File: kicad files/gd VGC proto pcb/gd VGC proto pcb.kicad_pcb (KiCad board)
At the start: 4 copper layers, 114.3 x 73.7 mm, 117 parts, among them J1 +5V_IN, J10 VID_OUT, J11 RCA MONO OUT, J12 Main Data Bus, J13 COMSYNC, J14 Mono-Color, J15 VBL, J16 RTC, J17 RCA Shunt Select, J18 RCA, J19 CREF, J2 Video Binary B, J20 RGB In, J21 CLK_14M, J22 Memory Control, J23 VGC Extra, J24 CLK_PH0, J25 Bald-Ext-1, J26 SYNC, J27 12V_IN, J28 -5V_In, J3 Aux Data Bus, J4 DAC RGB, J5 Video Binary G, J6 COMP_RGB, J7 Video Binary R, J8 RAM Addr Bus, J9 Composite Sync, Q1 BC817, Q2 BC817, Q3 BC817, U1 MIC5504-3.3YM5, U2 28.636360 MHz

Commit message: revision 1 routed and ready for fab
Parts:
- added REF**: OSHW-Logo2_7.3x6mm_SilkScreen, Symbol:OSHW-Logo2_7.3x6mm_SilkScreen, B.Cu at (190.5, 130.8)
- added REF**: KiCad-Logo2_5mm_SilkScreen, Symbol:KiCad-Logo2_5mm_SilkScreen, B.Cu at (152.4, 88.9)
- added svg2mod: G***, My Libraries:BE5v2, B.Cu at (172.7, 119.4)
- TP5: moved to B.Cu
- moved TF1 1.30 mm to (187.8, 115.2)
- moved TP5 1.28 mm to (95.8, 83.1)
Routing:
- net /R8-2: track 3.35 -> 2.57 mm
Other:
- board text added: "+12V"
- board text added: "+5V"
- board text added: "-5V"
- board text added: "0"
- board text added: "1"
- board text added: "1 1"
- board text added: "10"
- board text added: "11"
- board text added: "14M"
- board text added: "2"
- board text added: "28M"
- board text added: "3"
- board text added: "3.5DIK"
- board text added: "4"
- board text added: "5"
- board text added: "5V"
- board text added: "6"
- board text added: "7"
- board text added: "8"
- board text added: "9"
- board text added: "A2RW"
- board text added: "AD"
- board text added: "AD0"
- board text added: "AD1"
- board text added: "AD2"
- board text added: "AD3"
- board text added: "AD4"
- board text added: "AD5"
- board text added: "AD6"
- board text added: "AD7"
- board text added: "Aux Data"
- board text added: "BAUS12"
- board text added: "CBLU"
- board text added: "CGRN"
- board text added: "COM SYNC"
- board text added: "COM- SYNC"
- board text added: "COMP- SYN"
- board text added: "COMP_SYN"
- board text added: "CRED"
- board text added: "CREF.H"
- board text added: "CREF.L"
- board text added: "CSYN"
- board text added: "FLIP6"
- board text added: "Flip6"
- board text added: "Flip7"
- board text added: "Golden Delicious VGC Proto PCB v1 @baldengineer rev1"
- board text added: "H2"
- board text added: "H2-1"
- board text added: "H2-6"
- board text added: "H3"
- board text added: "H3-1"
- board text added: "H3-6"
- board text added: "H4"
- board text added: "H4-1"
- board text added: "H4-6"
- board text added: "HDSEL"
- board text added: "Hi Chat! Thank You! *rj was right"
- board text added: "IRQ"
- board text added: "L12"
- board text added: "L3"
- board text added: "L4"
- board text added: "M2SEL"
- board text added: "MC"
- board text added: "MD"
- board text added: "MD0"
- board text added: "MD1"
- board text added: "MD2"
- board text added: "MD3"
- board text added: "MD4"
- board text added: "MD5"
- board text added: "MD6"
- board text added: "MD7"
- board text added: "Main Data"
- board text added: "Mono Color"
- board text added: "N/C"
- board text added: "PH0"
- board text added: "RA"
- board text added: "RA0"
- board text added: "RA1"
- board text added: "RA2"
- board text added: "RA3"
- board text added: "RA4"
- board text added: "RA5"
- board text added: "RA6"
- board text added: "RA7"
- board text added: "RAM Addr"
- board text added: "RCA Out"
- board text added: "RCA Shunt"
- board text added: "RESET"
- board text added: "RGB"
- board text added: "RGB1"
- board text added: "RGB2"
- board text added: "RGB4"
- board text added: "RGB8"
- board text added: "RW"
- board text added: "STRETCH"
- board text added: "SYNC"
- board text added: "Stretch"
- board text added: "UC2-10"
- board text added: "UC2-3"
- board text added: "UC2-4"
- board text added: "UC2-5"
- board text added: "UG3-1"
- board text added: "UG3-5"
- board text added: "UG3-6"
- board text added: "UG3-7"
- board text added: "VBL"
- board text added: "VBL.L"
- board text added: "VID"

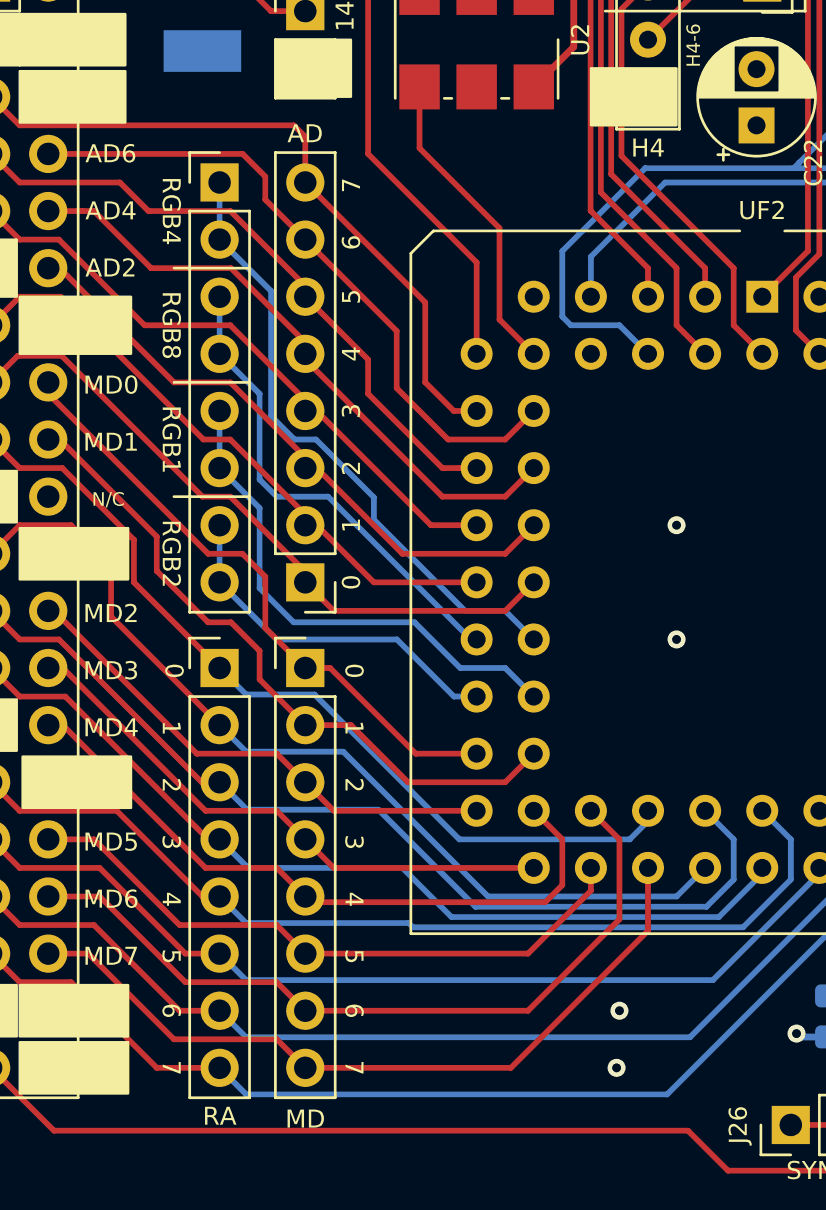
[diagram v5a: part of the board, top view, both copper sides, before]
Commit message: added some small vias for GND pours that missed
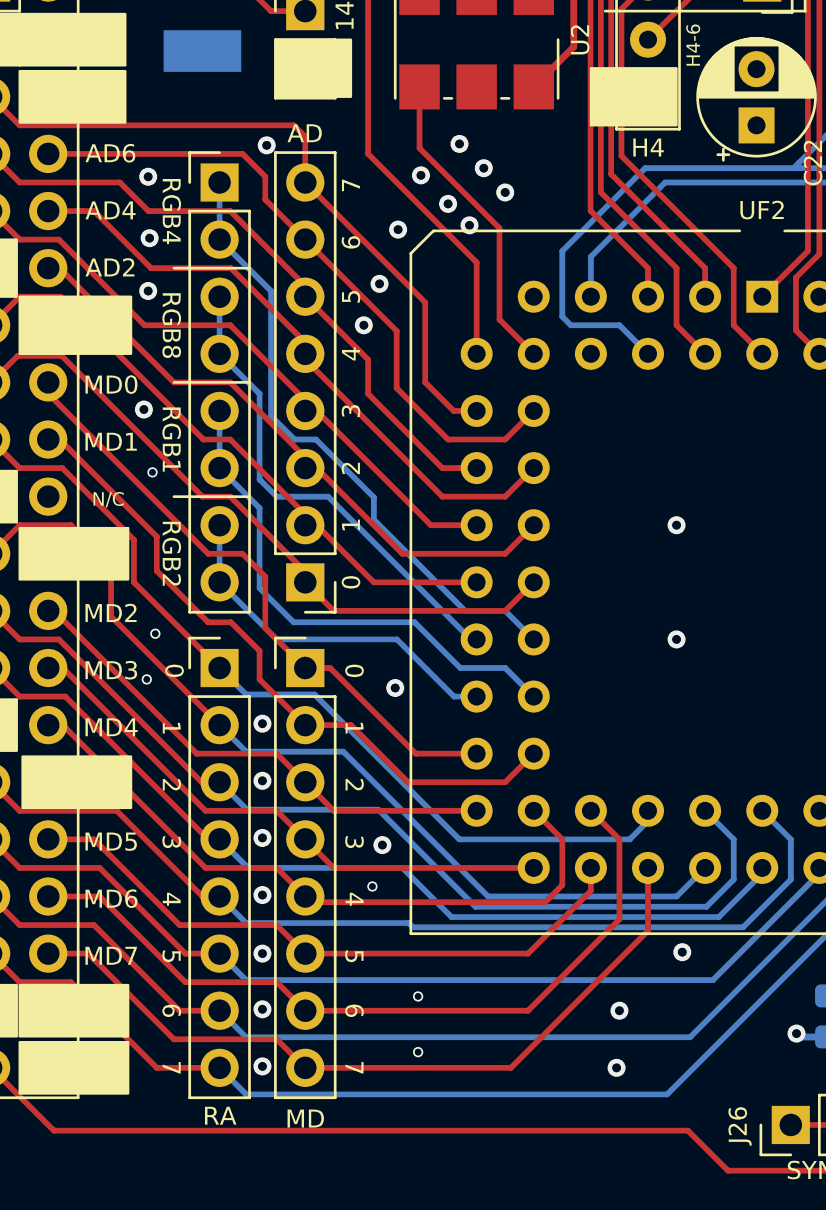
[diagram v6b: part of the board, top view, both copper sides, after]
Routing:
- net GND: vias 31 -> 61

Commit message: Added mounting to VGC board. PDF Of VGC schematic rev1. and created 6502 proto blank project.
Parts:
- removed REF**: OSHW-Logo2_7.3x6mm_SilkScreen, Symbol:OSHW-Logo2_7.3x6mm_SilkScreen
- removed REF**: KiCad-Logo2_5mm_SilkScreen, Symbol:KiCad-Logo2_5mm_SilkScreen
- removed svg2mod: G***, My Libraries:BE5v2
- added H5: MountingHole, MountingHole:MountingHole_2.7mm_M2.5, F.Cu at (193.1, 132.1)
- added H6: MountingHole, MountingHole:MountingHole_2.7mm_M2.5, F.Cu at (83.8, 132.1)
- added H7: MountingHole, MountingHole:MountingHole_2.7mm_M2.5, F.Cu at (193.1, 63.5)
- added H8: MountingHole, MountingHole:MountingHole_2.7mm_M2.5, F.Cu at (83.8, 63.5)
